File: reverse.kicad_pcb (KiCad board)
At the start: 2 copper layers, 40 x 29 mm, 19 parts, among them J1 AVR-ISP-6, Q1 DMG1012T-7, SW1 SW_Push, U1 ATtiny48-MMU

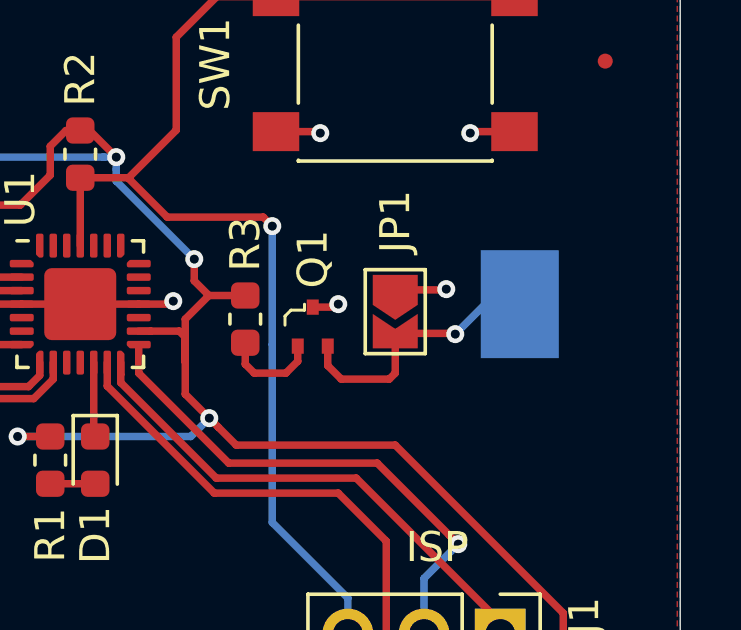
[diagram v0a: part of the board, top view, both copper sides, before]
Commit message: Fixed a problem with mosfet having drain and source reversed.
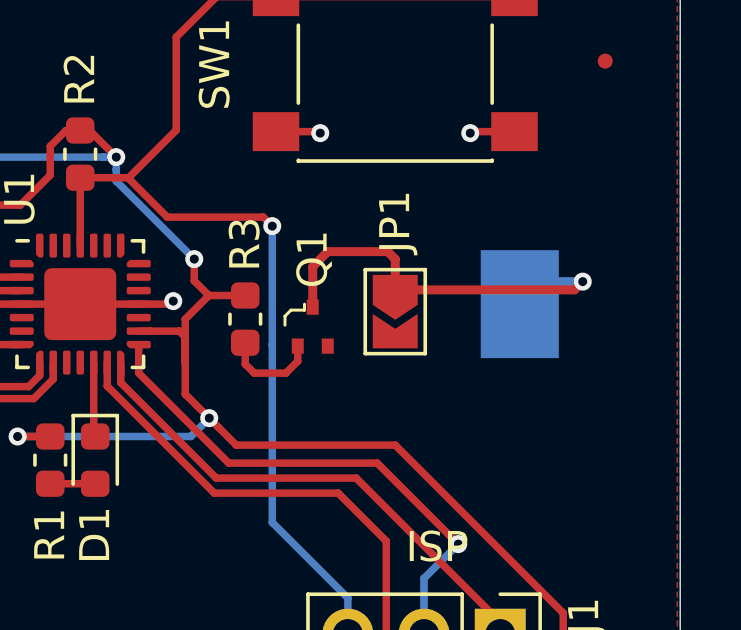
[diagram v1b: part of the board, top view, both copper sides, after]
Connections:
- JP1 pad 1: GND -> Net-(BT1-Pad2)
- JP1 pad 2: Net-(BT1-Pad2) -> GND
- Q1 pad 2: Net-(BT1-Pad2) -> GND
- Q1 pad 3: GND -> Net-(BT1-Pad2)
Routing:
- net Net-(BT1-Pad2): track 9.07 -> 14.2 mm
- net GND: track 13.1 -> 10.5 mm, vias 7 -> 5
